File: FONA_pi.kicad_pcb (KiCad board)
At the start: 2 copper layers, 101.6 x 68.6 mm, 24 parts, among them J1 Conn_01x20_Socket, J10 Conn_01x04_Pin, J11 Conn_01x20_Socket, J12 Conn_01x20_Socket, J13 Conn_01x06_Socket, J14 Conn_01x06_Socket, J15 Conn_01x06_Socket, J2 Conn_02x20_Odd_Even, J3 Conn_01x20_Socket, J4 Conn_01x20_Socket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

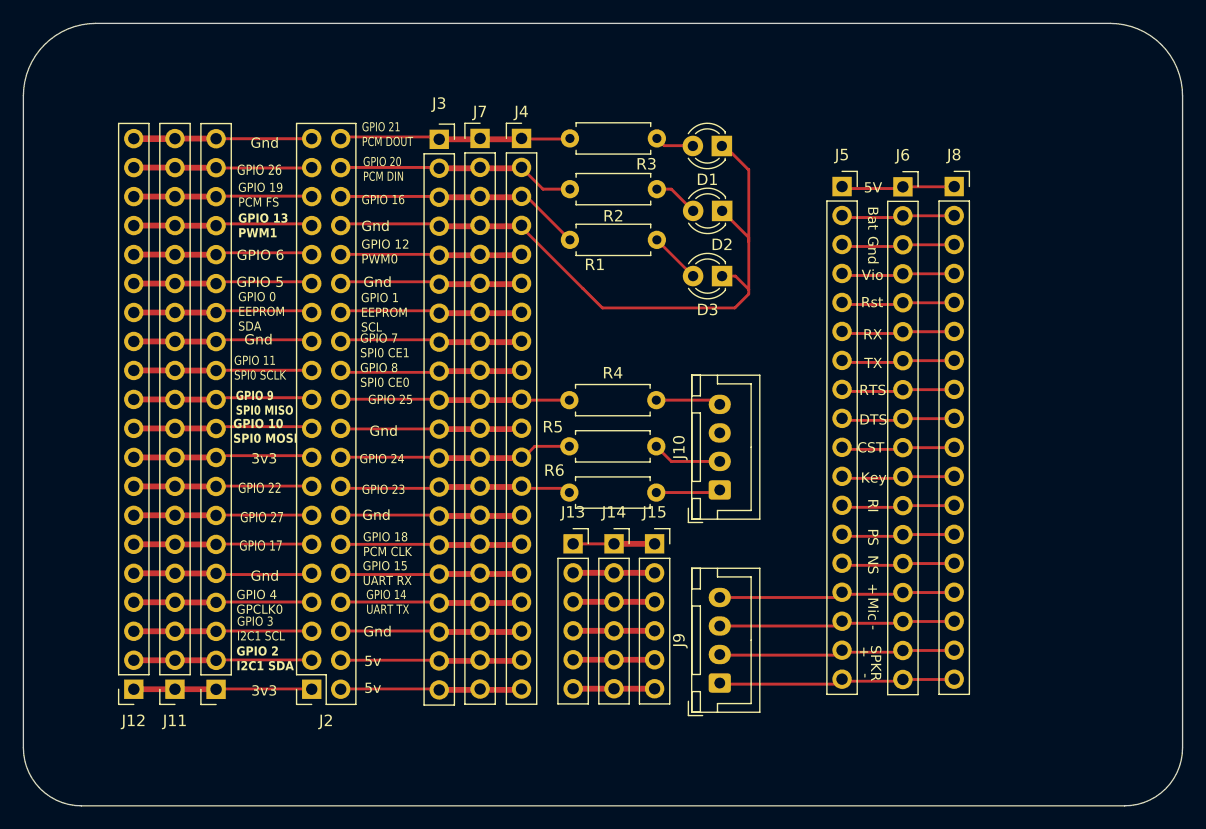
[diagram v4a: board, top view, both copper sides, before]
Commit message: Added power and ground rails
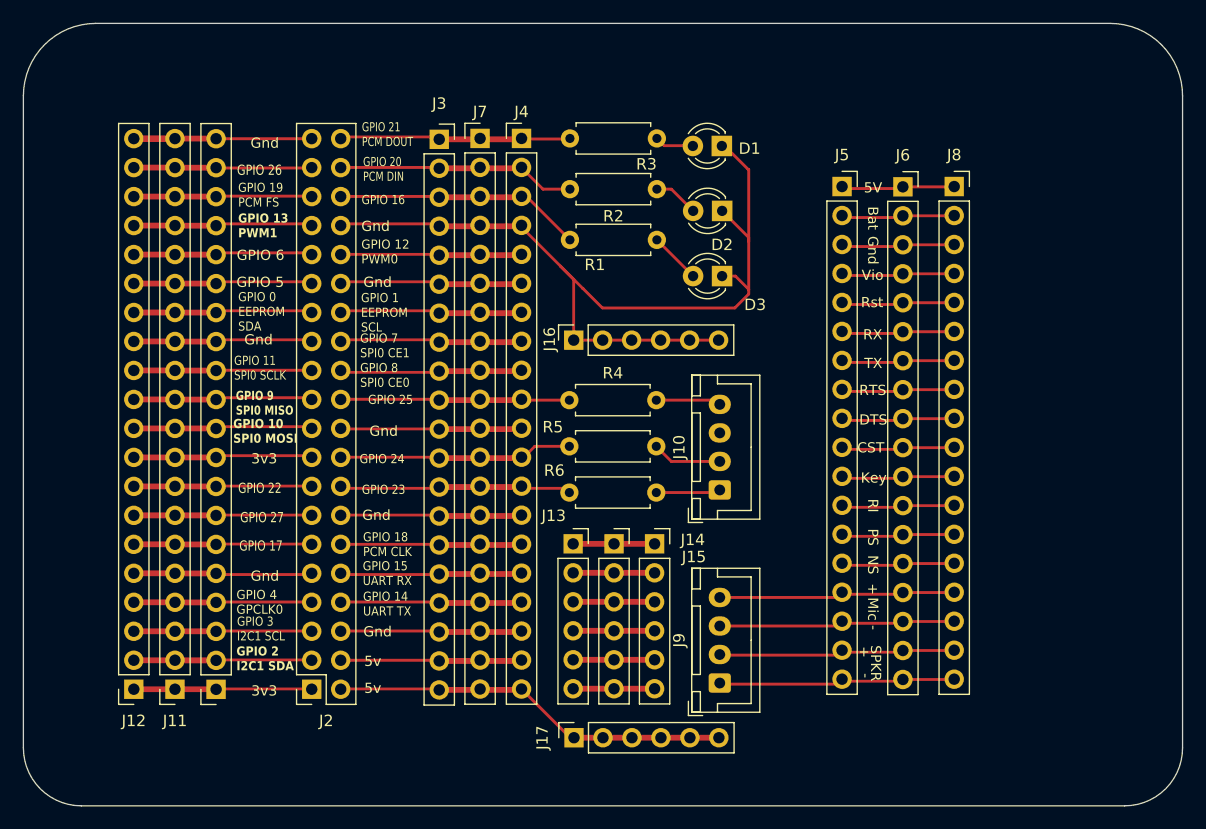
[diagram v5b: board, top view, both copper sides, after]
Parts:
- added J16: Conn_01x06_Socket, Connector_PinSocket_2.54mm:PinSocket_1x06_P2.54mm_Vertical, F.Cu at (124.4, 78.6)
- added J17: Conn_01x06_Socket, Connector_PinSocket_2.54mm:PinSocket_1x06_P2.54mm_Vertical, F.Cu at (124.5, 113.4)
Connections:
- J10 pad 3: Net-(J1-Pin_1) -> unconnected-(J10-Pin_3-Pad3)
- J2 pad 10: Net-(J13-Pin_2) -> Net-(J2-Pin_10)
- J2 pad 12: Net-(J13-Pin_1) -> Net-(J2-Pin_12)
- J2 pad 2: Net-(J13-Pin_6) -> Net-(J17-Pin_1)
- J2 pad 4: Net-(J13-Pin_5) -> Net-(J2-Pin_4)
- J2 pad 6: Net-(J13-Pin_4) -> Net-(J2-Pin_6)
- J2 pad 8: Net-(J13-Pin_3) -> Net-(J2-Pin_8)
- J3 pad 15: Net-(J13-Pin_1) -> Net-(J2-Pin_12)
- J3 pad 16: Net-(J13-Pin_2) -> Net-(J2-Pin_10)
- J3 pad 17: Net-(J13-Pin_3) -> Net-(J2-Pin_8)
- J3 pad 18: Net-(J13-Pin_4) -> Net-(J2-Pin_6)
- J3 pad 19: Net-(J13-Pin_5) -> Net-(J2-Pin_4)
- J3 pad 20: Net-(J13-Pin_6) -> Net-(J17-Pin_1)
- J4 pad 15: Net-(J13-Pin_1) -> Net-(J2-Pin_12)
- J4 pad 16: Net-(J13-Pin_2) -> Net-(J2-Pin_10)
- J4 pad 17: Net-(J13-Pin_3) -> Net-(J2-Pin_8)
- J4 pad 18: Net-(J13-Pin_4) -> Net-(J2-Pin_6)
- J4 pad 19: Net-(J13-Pin_5) -> Net-(J2-Pin_4)
- J4 pad 20: Net-(J13-Pin_6) -> Net-(J17-Pin_1)
- J7 pad 15: Net-(J13-Pin_1) -> Net-(J2-Pin_12)
- J7 pad 16: Net-(J13-Pin_2) -> Net-(J2-Pin_10)
- J7 pad 17: Net-(J13-Pin_3) -> Net-(J2-Pin_8)
- J7 pad 18: Net-(J13-Pin_4) -> Net-(J2-Pin_6)
- J7 pad 19: Net-(J13-Pin_5) -> Net-(J2-Pin_4)
- J7 pad 20: Net-(J13-Pin_6) -> Net-(J17-Pin_1)
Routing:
- net Net-(J17-Pin_1): track 0.00 -> 35.0 mm
- net Net-(D1-K): track 59.6 -> 79.3 mm
- net Net-(J13-Pin_1): track 23.2 -> 7.14 mm
- net Net-(J13-Pin_5): track 23.1 -> 7.14 mm
- net Net-(J2-Pin_4): track 0.00 -> 15.9 mm
- net Net-(J2-Pin_12): track 0.00 -> 15.9 mm
- net Net-(J2-Pin_8): track 0.00 -> 15.8 mm
- net Net-(J2-Pin_6): track 0.00 -> 15.8 mm
- net Net-(J13-Pin_6): track 23.0 -> 7.14 mm
- net Net-(J13-Pin_4): track 23.0 -> 7.14 mm
- net Net-(J13-Pin_3): track 23.0 -> 7.14 mm
- net Net-(J2-Pin_10): track 0.00 -> 15.8 mm
- net Net-(J13-Pin_2): track 23.0 -> 7.14 mm

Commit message: Added solder jumpers, ran them to GPIO pins.  Connected FONA pins to Pi, UART RX/TX, RI, NS, PS, etc to various GPIOs
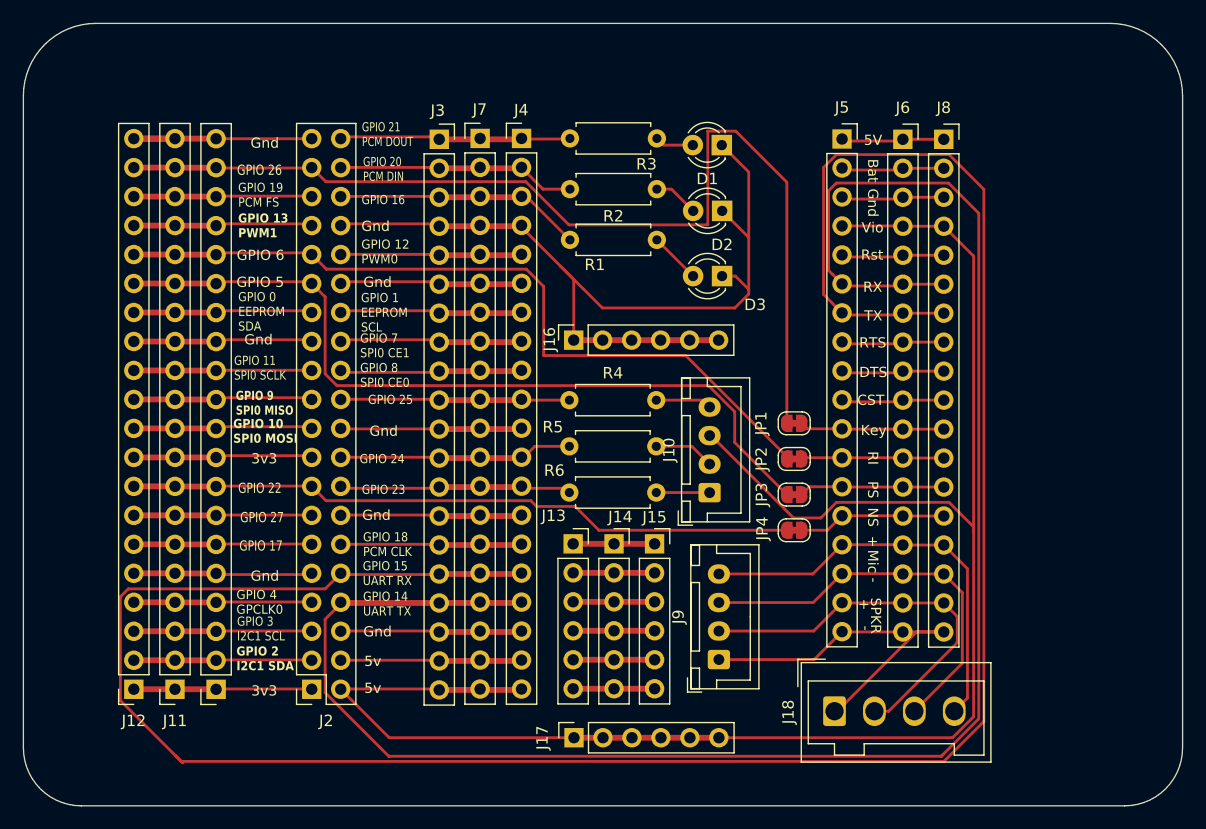
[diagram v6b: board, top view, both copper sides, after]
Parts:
- added J18: Conn_01x04, Connector_Wago:Wago_734-134_1x04_P3.50mm_Vertical, F.Cu at (147.3, 111.1)
- added JP1: Jumper_2_Bridged, Jumper:SolderJumper-2_P1.3mm_Bridged_RoundedPad1.0x1.5mm, F.Cu at (143.8, 85.9)
- added JP2: Jumper_2_Bridged, Jumper:SolderJumper-2_P1.3mm_Bridged_RoundedPad1.0x1.5mm, F.Cu at (143.8, 89.0)
- added JP3: Jumper_2_Bridged, Jumper:SolderJumper-2_P1.3mm_Bridged_RoundedPad1.0x1.5mm, F.Cu at (143.8, 92.1)
- added JP4: Jumper_2_Bridged, Jumper:SolderJumper-2_P1.3mm_Bridged_RoundedPad1.0x1.5mm, F.Cu at (143.8, 95.2)
- moved J8 4.24 mm to (156.9, 61.0)
- moved J6 4.17 mm to (153.3, 61.0)
- moved J5 4.17 mm to (148.0, 60.9)
- moved J9 2.06 mm to (137.2, 106.6)
- moved J10 0.92 mm to (136.3, 91.9)
- moved D1 0.08 mm to (137.4, 61.5)
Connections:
- J10 pad 3: unconnected-(J10-Pin_3-Pad3) -> Net-(J10-Pin_3)
- J17 pad 1: Net-(J17-Pin_1) -> Net-(J10-Pin_3)
- J17 pad 2: Net-(J17-Pin_1) -> Net-(J10-Pin_3)
- J17 pad 3: Net-(J17-Pin_1) -> Net-(J10-Pin_3)
- J17 pad 4: Net-(J17-Pin_1) -> Net-(J10-Pin_3)
- J17 pad 5: Net-(J17-Pin_1) -> Net-(J10-Pin_3)
- J17 pad 6: Net-(J17-Pin_1) -> Net-(J10-Pin_3)
- J2 pad 2: Net-(J17-Pin_1) -> Net-(J10-Pin_3)
- J3 pad 20: Net-(J17-Pin_1) -> Net-(J10-Pin_3)
- J4 pad 20: Net-(J17-Pin_1) -> Net-(J10-Pin_3)
- J5 pad 4: Net-(J5-Pin_4) -> Net-(J10-Pin_3)
- J5 pad 6: Net-(J5-Pin_6) -> Net-(J2-Pin_8)
- J5 pad 7: Net-(J5-Pin_7) -> Net-(J2-Pin_10)
- J6 pad 4: Net-(J5-Pin_4) -> Net-(J10-Pin_3)
- J6 pad 6: Net-(J5-Pin_6) -> Net-(J2-Pin_8)
- J6 pad 7: Net-(J5-Pin_7) -> Net-(J2-Pin_10)
- J7 pad 20: Net-(J17-Pin_1) -> Net-(J10-Pin_3)
- J8 pad 4: Net-(J5-Pin_4) -> Net-(J10-Pin_3)
- J8 pad 6: Net-(J5-Pin_6) -> Net-(J2-Pin_8)
- J8 pad 7: Net-(J5-Pin_7) -> Net-(J2-Pin_10)
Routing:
- net Net-(J2-Pin_10): track 15.8 -> 209.3 mm
- net Net-(J2-Pin_8): track 15.8 -> 185.6 mm
- net Net-(J10-Pin_3): track 0.00 -> 155.1 mm
- net Net-(J1-Pin_19): track 15.7 -> 90.6 mm
- net Net-(J1-Pin_15): track 15.9 -> 70.7 mm
- net Net-(J1-Pin_16): track 15.9 -> 68.6 mm
- net Net-(J1-Pin_8): track 15.9 -> 59.1 mm
- net Net-(J17-Pin_1): track 35.0 -> 0.00 mm
- net Net-(J18-Pin_4): track 20.4 -> 36.7 mm
- net Net-(J18-Pin_3): track 20.4 -> 35.2 mm
- net Net-(J18-Pin_2): track 20.4 -> 34.4 mm
- net Net-(J18-Pin_1): track 20.3 -> 33.2 mm
- net Net-(J5-Pin_7): track 9.20 -> 0.00 mm
- net Net-(J5-Pin_6): track 9.20 -> 0.00 mm
- net Net-(J5-Pin_4): track 9.20 -> 0.00 mm
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
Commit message: Masked any traces that were going in between Pi pin solder pads
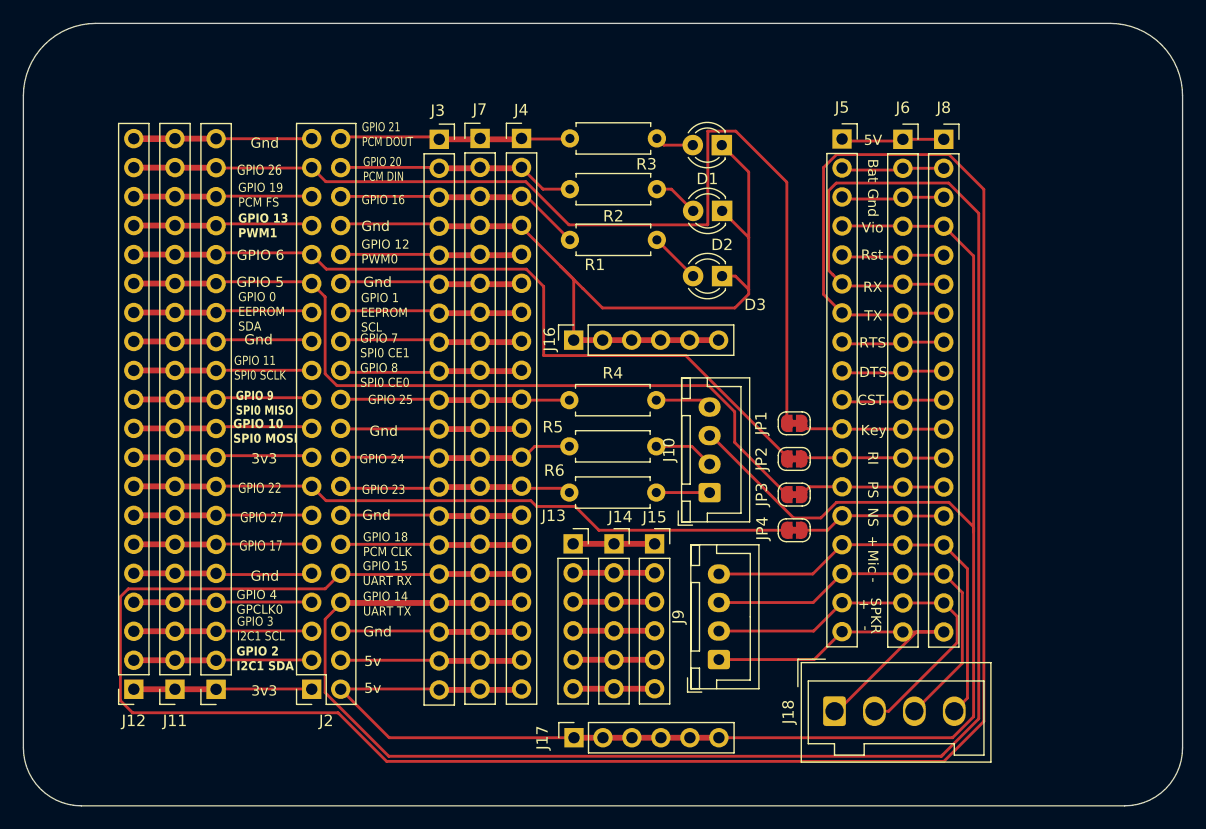
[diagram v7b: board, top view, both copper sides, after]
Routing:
- net Net-(J2-Pin_10): track 209.3 -> 208.4 mm
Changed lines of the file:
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@@
     )
   )
+  (gr_rect (start 84.7852 59.9186) (end 94.0054 74.9046)
+    (stroke (width 0.15) (type solid)) (fill solid) (layer "F.Mask"))
   (gr_rect (start 125.2474 112.5474) (end 136.6266 114.3)
     (stroke (width 0.15) (type solid)) (fill solid) (layer "F.Mask"))
+  (gr_rect (start 111.7346 82.931) (end 120.777 92.2528)
+    (stroke (width 0.15) (type solid)) (fill solid) (layer "F.Mask"))
   (gr_rect (start 125.222 77.6732) (end 136.7028 79.502)
     (stroke (width 0.15) (type solid)) (fill solid) (layer "F.Mask"))
-  (gr_rect (start 111.9124 60.1218) (end 120.6246 110.1852)
-    (stroke (width 0.2) (type solid)) (fill solid) (layer "F.Mask"))
+  (gr_rect (start 85.3694 100.5586) (end 93.9292 110.0074)
+    (stroke (width 0.15) (type solid)) (fill solid) (layer "F.Mask"))
+  (gr_rect (start 111.6584 93.0402) (end 120.8532 110.0582)
+    (stroke (width 0.15) (type solid)) (fill solid) (layer "F.Mask"))
+  (gr_rect (start 111.7854 77.724) (end 120.6754 82.0166)
+    (stroke (width 0.15) (type solid)) (fill solid) (layer "F.Mask"))
   (gr_rect (start 125.1458 95.5548) (end 130.7846 109.728)
     (stroke (width 0.15) (type solid)) (fill solid) (layer "F.Mask"))
-  (gr_rect (start 84.9376 59.8678) (end 93.9292 110.0074)
-    (stroke (width 0.15) (type solid)) (fill solid) (layer "F.Mask"))
+  (gr_rect (start 111.6838 64.9732) (end 120.7262 71.9074)
+    (stroke (width 0.15) (type solid)) (fill solid) (layer "F.Mask"))
+  (gr_rect (start 111.7854 60.1472) (end 120.7262 71.9074)
+    (stroke (width 0.15) (type solid)) (fill none) (layer "F.Mask"))
   (gr_rect (start 83.8708 59.2582) (end 83.947 59.2582)
     (stroke (width 0.15) (type default)) (fill none) (layer "F.Mask"))
+  (gr_rect (start 111.7854 60.1472) (end 120.7262 64.2366)
+    (stroke (width 0.15) (type solid)) (fill solid) (layer "F.Mask"))
+  (gr_rect (start 111.8108 72.8218) (end 120.777 74.4474)
+    (stroke (width 0.15) (type solid)) (fill solid) (layer "F.Mask"))
+  (gr_rect (start 84.6074 77.5716) (end 93.98 99.5426)
+    (stroke (width 0.15) (type solid)) (fill solid) (layer "F.Mask"))
+  (gr_rect (start 116.2939 72.8218) (end 116.2939 72.8218)
+    (stroke (width 0.15) (type solid)) (fill none) (layer "F.Mask"))
   (gr_line (start 177.8 57.15) (end 177.8 114.3)
     (stroke (width 0.1) (type default)) (layer "Edge.Cuts"))
@@
   (segment (start 116.2304 96.52) (end 112.649 96.52) (width 0.508) (layer "F.Cu") (net 58))
   (segment (start 112.589 96.46) (end 112.649 96.52) (width 0.25) (layer "F.Cu") (net 58))
-  (segment (start 85.390699 100.365) (end 102.648 100.365) (width 0.25) (layer "F.Cu") (net 59))
-  (segment (start 156.8776 115.4866) (end 90.0358 115.4866) (width 0.25) (layer "F.Cu") (net 59))
+  (segment (start 156.8776 115.4866) (end 160.3866 111.9776) (width 0.25) (layer "F.Cu") (net 59))
+  (segment (start 108.041503 115.4866) (end 156.8776 115.4866) (width 0.25) (layer "F.Cu") (net 59))
+  (segment (start 160.3866 65.354499) (end 157.331701 62.2996) (width 0.25) (layer "F.Cu") (net 59))
   (segment (start 152.6006 76.3524) (end 148.0006 76.3524) (width 0.25) (layer "F.Cu") (net 59))
-  (segment (start 146.33 63.437899) (end 147.468299 62.2996) (width 0.25) (layer "F.Cu") (net 59))
+  (segment (start 157.331701 62.2996) (end 147.468299 62.2996) (width 0.25) (layer "F.Cu") (net 59))
   (segment (start 112.649 99.06) (end 116.2304 99.06) (width 0.508) (layer "F.Cu") (net 59))
-  (segment (start 147.955 76.1746) (end 146.33 74.5496) (width 0.25) (layer "F.Cu") (net 59))
-  (segment (start 84.7024 101.053299) (end 85.390699 100.365) (width 0.25) (layer "F.Cu") (net 59))
-  (segment (start 160.3866 111.9776) (end 156.8776 115.4866) (width 0.25) (layer "F.Cu") (net 59))
+  (segment (start 84.7024 101.053299) (end 84.7024 110.1532) (width 0.25) (layer "F.Cu") (net 59))
+  (segment (start 85.390699 100.365) (end 84.7024 101.053299) (width 0.25) (layer "F.Cu") (net 59))
+  (segment (start 84.7024 110.1532) (end 85.7758 111.2266) (width 0.25) (layer "F.Cu") (net 59))
   (segment (start 156.8704 76.2) (end 153.2864 76.2) (width 0.25) (layer "F.Cu") (net 59))
-  (segment (start 89.535 114.9858) (end 84.7024 110.1532) (width 0.25) (layer "F.Cu") (net 59))
-  (segment (start 146.33 74.5496) (end 146.33 63.437899) (width 0.25) (layer "F.Cu") (net 59))
-  (segment (start 147.468299 62.2996) (end 157.331701 62.2996) (width 0.25) (layer "F.Cu") (net 59))
-  (segment (start 157.331701 62.2996) (end 160.3866 65.354499) (width 0.25) (layer "F.Cu") (net 59))
-  (segment (start 84.7024 110.1532) (end 84.7024 101.053299) (width 0.25) (layer "F.Cu") (net 59))
+  (segment (start 85.7758 111.2266) (end 103.781503 111.2266) (width 0.25) (layer "F.Cu") (net 59))
+  (segment (start 146.33 74.5496) (end 147.955 76.1746) (width 0.25) (layer "F.Cu") (net 59))
   (segment (start 116.2304 99.06) (end 119.8626 99.06) (width 0.508) (layer "F.Cu") (net 59))
-  (segment (start 102.648 100.365) (end 104.013 99) (width 0.25) (layer "F.Cu") (net 59))
-  (segment (start 90.0358 115.4866) (end 89.535 114.9858) (width 0.25) (layer "F.Cu") (net 59))
-  (segment (start 160.3866 65.354499) (end 160.3866 111.9776) (width 0.25) (layer "F.Cu") (net 59))
+  (segment (start 146.33 63.437899) (end 146.33 74.5496) (width 0.25) (layer "F.Cu") (net 59))
+  (segment (start 103.781503 111.2266) (end 108.041503 115.4866) (width 0.25) (layer "F.Cu") (net 59))
+  (segment (start 160.3866 111.9776) (end 160.3866 65.354499) (width 0.25) (layer "F.Cu") (net 59))
+  (segment (start 102.648 100.365) (end 85.390699 100.365) (width 0.25) (layer "F.Cu") (net 59))
+  (segment (start 147.468299 62.2996) (end 146.33 63.437899) (width 0.25) (layer "F.Cu") (net 59))
   (segment (start 103.9876 99.1088) (end 112.589 99.1088) (width 0.25) (layer "F.Cu") (net 59))
-  (segment (start 90.17 115.6208) (end 89.535 114.9858) (width 0.25) (layer "F.Cu") (net 59))
+  (segment (start 104.013 99) (end 102.648 100.365) (width 0.25) (layer "F.Cu") (net 59))
   (segment (start 157.287501 64.7954) (end 147.447 64.7954) (width 0.25) (layer "F.Cu") (net 60))
   (segment (start 148.0006 73.8124) (end 152.6006 73.8124) (width 0.25) (layer "F.Cu") (net 60))

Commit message: little fixes, tracks, etc.
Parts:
- moved J9 0.81 mm to (136.3, 106.6)
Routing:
- net Net-(J2-Pin_8): track 185.6 -> 161.2 mm
- net Net-(J10-Pin_3): track 155.1 -> 139.3 mm
- net Net-(J1-Pin_16): track 68.6 -> 67.6 mm
- net Net-(J1-Pin_19): track 90.6 -> 91.3 mm
